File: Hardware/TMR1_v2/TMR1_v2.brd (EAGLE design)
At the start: 41 x 48.3 mm, 46 parts, among them J1 455-1750-1-ND, J2 455-1750-1-ND, U1 ATMEGA328P_TQFP, U2 MCP79410I/SN, Y1 32.768kHz

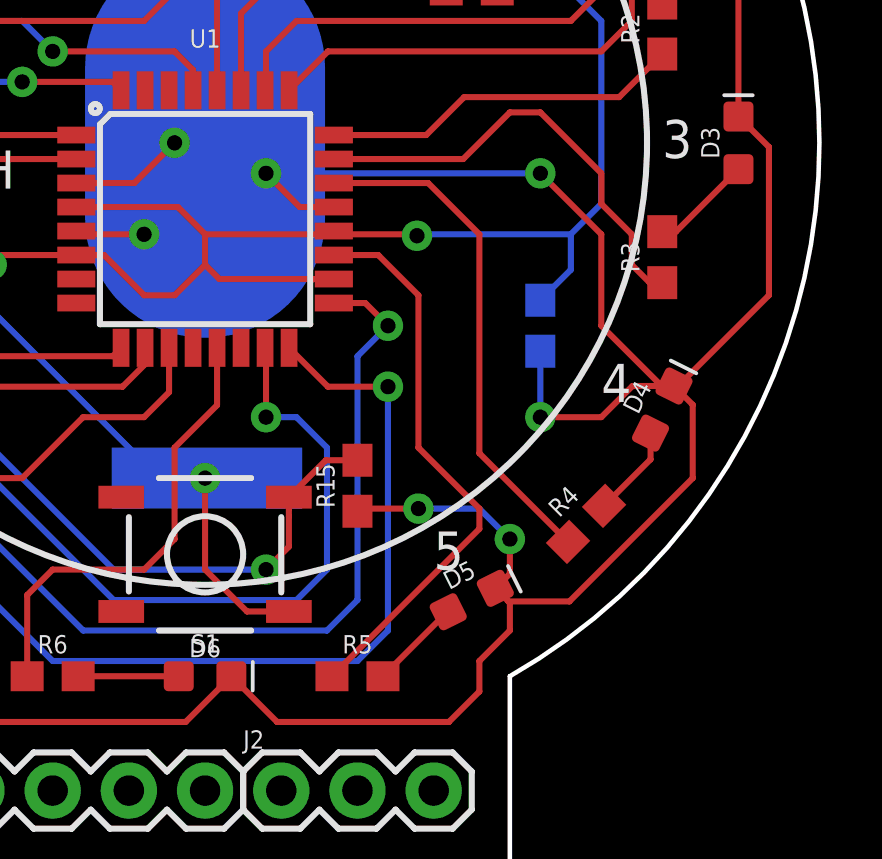
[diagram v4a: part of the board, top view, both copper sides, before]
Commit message: correction for the analogic pings ADC6-7 with MISO-SCK, HW and SW
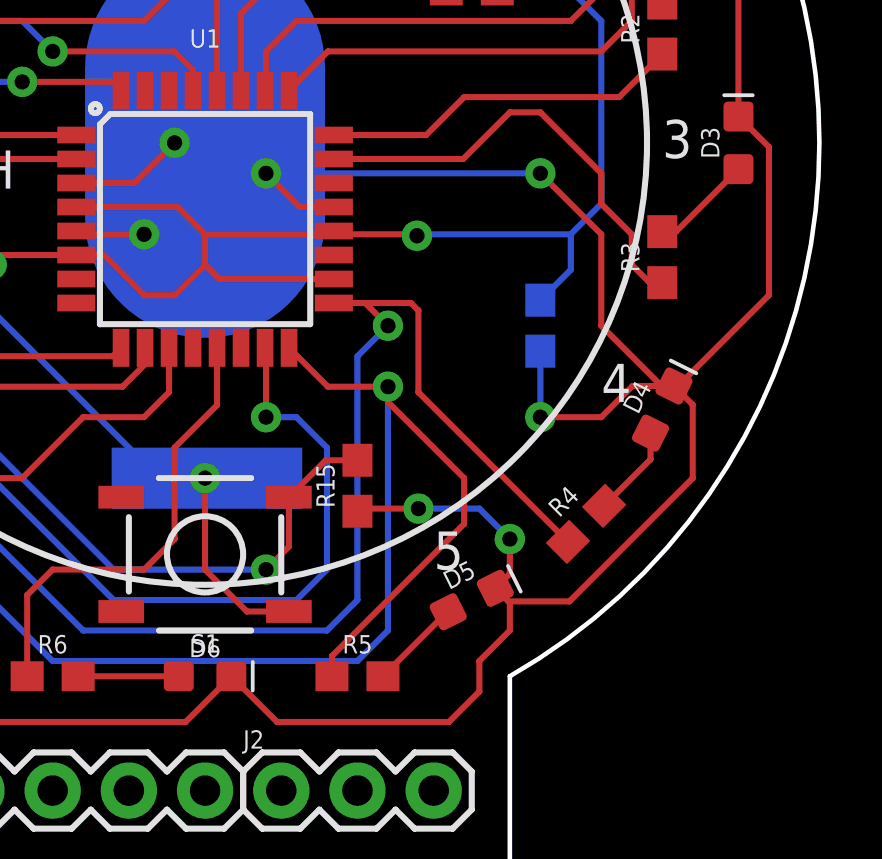
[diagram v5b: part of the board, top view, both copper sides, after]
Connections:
- removed net D4: R4.1, U1.22
- removed net D5: R5.1, U1.19
- new net D4_NA: U1.22
- new net D5_NA: U1.19
- net MISO: now also R5.1
- net SCK: now also R4.1
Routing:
- net D5: track 19.0 -> 0.00 mm
- net D4: track 17.0 -> 0.00 mm
- net MISO: track 42.4 -> 54.9 mm
- net SCK: track 42.0 -> 53.7 mm
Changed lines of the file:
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@@
 <layers>
 <layer number="1" name="Top" color="4" fill="1" visible="yes" active="yes"/>
-<layer number="16" name="Bottom" color="1" fill="1" visible="yes" active="yes"/>
+<layer number="16" name="Bottom" color="1" fill="1" visible="no" active="yes"/>
 <layer number="17" name="Pads" color="2" fill="1" visible="yes" active="yes"/>
 <layer number="18" name="Vias" color="2" fill="1" visible="yes" active="yes"/>
@@
 <layer number="20" name="Dimension" color="24" fill="1" visible="yes" active="yes"/>
 <layer number="21" name="tPlace" color="7" fill="1" visible="yes" active="yes"/>
-<layer number="22" name="bPlace" color="7" fill="1" visible="yes" active="yes"/>
+<layer number="22" name="bPlace" color="7" fill="1" visible="no" active="yes"/>
 <layer number="23" name="tOrigins" color="15" fill="1" visible="yes" active="yes"/>
-<layer number="24" name="bOrigins" color="15" fill="1" visible="yes" active="yes"/>
+<layer number="24" name="bOrigins" color="15" fill="1" visible="no" active="yes"/>
 <layer number="25" name="tNames" color="7" fill="1" visible="yes" active="yes"/>
-<layer number="26" name="bNames" color="7" fill="1" visible="yes" active="yes"/>
-<layer number="27" name="tValues" color="7" fill="1" visible="yes" active="yes"/>
-<layer number="28" name="bValues" color="7" fill="1" visible="yes" active="yes"/>
+<layer number="26" name="bNames" color="7" fill="1" visible="no" active="yes"/>
+<layer number="27" name="tValues" color="7" fill="1" visible="no" active="yes"/>
+<layer number="28" name="bValues" color="7" fill="1" visible="no" active="yes"/>
 <layer number="29" name="tStop" color="7" fill="3" visible="no" active="yes"/>
 <layer number="30" name="bStop" color="7" fill="6" visible="no" active="yes"/>
@@
 <layer number="38" name="bTest" color="7" fill="1" visible="no" active="yes"/>
 <layer number="39" name="tKeepout" color="4" fill="11" visible="yes" active="yes"/>
-<layer number="40" name="bKeepout" color="1" fill="11" visible="yes" active="yes"/>
+<layer number="40" name="bKeepout" color="1" fill="11" visible="no" active="yes"/>
 <layer number="41" name="tRestrict" color="4" fill="10" visible="yes" active="yes"/>
-<layer number="42" name="bRestrict" color="1" fill="10" visible="yes" active="yes"/>
+<layer number="42" name="bRestrict" color="1" fill="10" visible="no" active="yes"/>
 <layer number="43" name="vRestrict" color="2" fill="10" visible="no" active="yes"/>
-<layer number="44" name="Drills" color="7" fill="1" visible="yes" active="yes"/>
+<layer number="44" name="Drills" color="7" fill="1" visible="no" active="yes"/>
 <layer number="45" name="Holes" color="7" fill="1" visible="yes" active="yes"/>
 <layer number="46" name="Milling" color="3" fill="1" visible="no" active="yes"/>
@@
 <layer number="50" name="dxf" color="7" fill="1" visible="no" active="no"/>
 <layer number="51" name="tDocu" color="7" fill="1" visible="yes" active="yes"/>
-<layer number="52" name="bDocu" color="7" fill="1" visible="yes" active="yes"/>
+<layer number="52" name="bDocu" color="7" fill="1" visible="no" active="yes"/>
 <layer number="53" name="tGND_GNDA" color="7" fill="9" visible="no" active="no"/>
 <layer number="54" name="bGND_GNDA" color="1" fill="9" visible="no" active="no"/>
@@
 <wire x1="28.2" y1="18.5674" x2="29.4954" y2="17.272" width="0.2032" layer="1"/>
 <wire x1="29.4954" y1="17.272" x2="31.496" y2="17.272" width="0.2032" layer="1"/>
+<contactref element="R5" pad="1"/>
+<wire x1="29.63" y1="7.62" x2="29.63" y2="8.294" width="0.2032" layer="1"/>
+<wire x1="34.036" y1="12.7" x2="34.036" y2="14.224" width="0.2032" layer="1"/>
+<wire x1="34.036" y1="14.224" x2="31.496" y2="16.764" width="0.2032" layer="1"/>
+<wire x1="31.496" y1="16.764" x2="31.496" y2="17.272" width="0.2032" layer="1"/>
+<wire x1="29.63" y1="8.294" x2="34.036" y2="12.7" width="0.2032" layer="1"/>
 </signal>
 <signal name="SCK">
@@
 <wire x1="29.464" y1="9.144" x2="21.336" y2="9.144" width="0.2032" layer="16"/>
 <wire x1="21.336" y1="9.144" x2="11.684" y2="18.796" width="0.2032" layer="16"/>
+<wire x1="30.74" y1="20.06" x2="32.264" y2="20.06" width="0.2032" layer="1"/>
+<wire x1="32.512" y1="19.812" x2="32.264" y2="20.06" width="0.2032" layer="1"/>
+<contactref element="R4" pad="1"/>
+<wire x1="37.49895625" y1="12.09895625" x2="32.512" y2="17.0859125" width="0.2032" layer="1"/>
+<wire x1="32.512" y1="17.0859125" x2="32.512" y2="19.812" width="0.2032" layer="1"/>
 </signal>
 <signal name="D1">
@@
 <wire x1="35.56" y1="26.416" x2="34.004" y2="24.86" width="0.2032" layer="1"/>
 </signal>
-<signal name="D4">
-<contactref element="R4" pad="1"/>
+<signal name="D4_NA">
 <contactref element="U1" pad="22"/>
-<wire x1="37.49895625" y1="12.09895625" x2="34.544" y2="15.0539125" width="0.2032" layer="1"/>
-<wire x1="32.836" y1="24.06" x2="29.6926" y2="24.06" width="0.2032" layer="1"/>
-<wire x1="34.544" y1="15.0539125" x2="34.544" y2="22.352" width="0.2032" layer="1"/>
-<wire x1="34.544" y1="22.352" x2="32.836" y2="24.06" width="0.2032" layer="1"/>
-</signal>
-<signal name="D5">
-<contactref element="R5" pad="1"/>
-<contactref element="U1" pad="19"/>
-<wire x1="29.63" y1="7.62" x2="34.544" y2="12.534" width="0.2032" layer="1"/>
-<wire x1="34.544" y1="12.534" x2="34.544" y2="13.208" width="0.2032" layer="1"/>
-<wire x1="34.544" y1="13.208" x2="32.512" y2="15.24" width="0.2032" layer="1"/>
-<wire x1="32.512" y1="15.24" x2="32.512" y2="20.32" width="0.2032" layer="1"/>
-<wire x1="31.172" y1="21.66" x2="29.6926" y2="21.66" width="0.2032" layer="1"/>
-<wire x1="32.512" y1="20.32" x2="31.172" y2="21.66" width="0.2032" layer="1"/>
 </signal>
 <signal name="D6">
@@
 <wire x1="32.805" y1="32.385" x2="33.44" y2="33.02" width="0.2032" layer="1"/>
 </signal>
+<signal name="D5_NA">
+<contactref element="U1" pad="19"/>
+</signal>
 </signals>
